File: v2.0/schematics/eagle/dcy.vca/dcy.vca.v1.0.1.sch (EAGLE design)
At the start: 104 parts, among them IC1 LM324N, IC2 4001N, IC3 TL074P, IC4 4001N, IC5 LM324N, IC6 TL074P

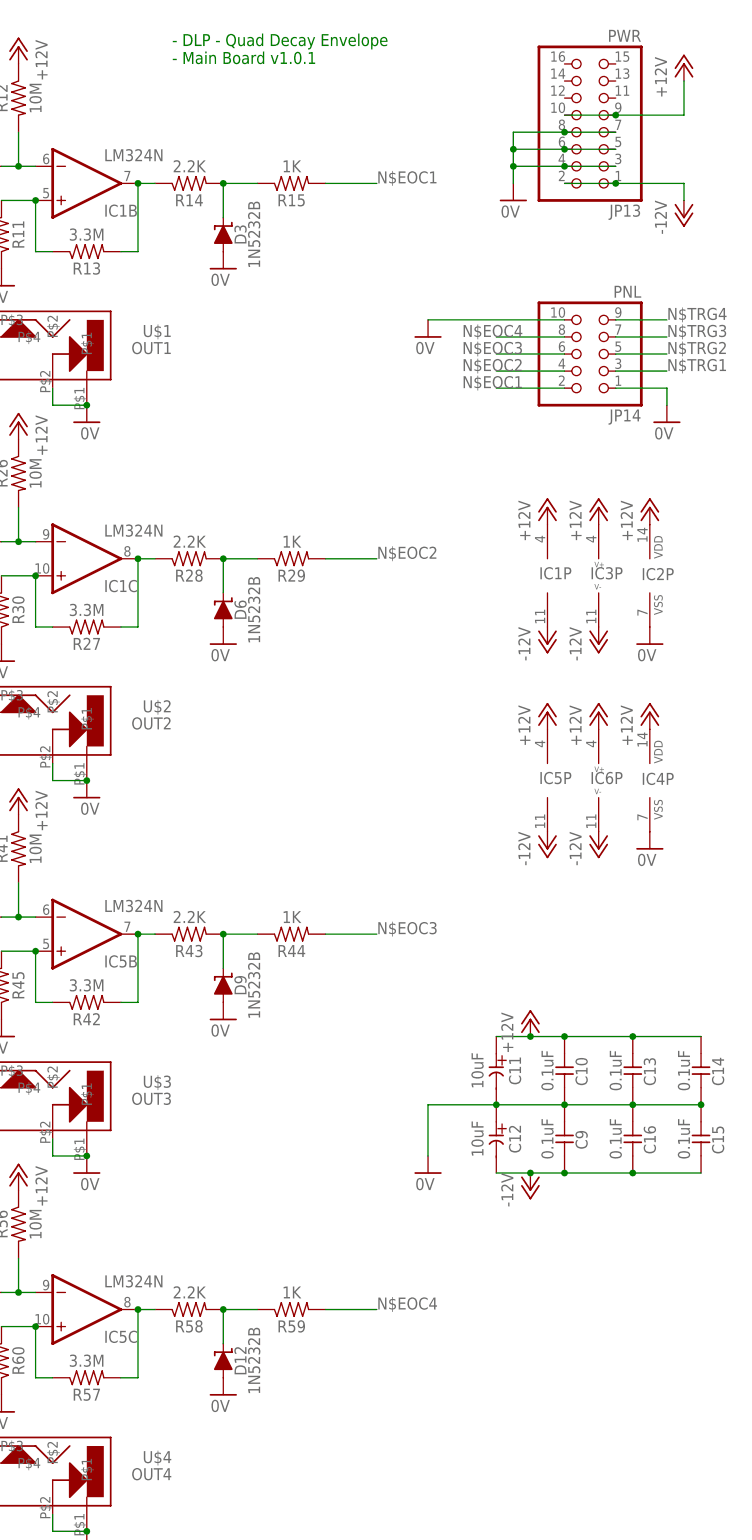
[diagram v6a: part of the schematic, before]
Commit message: Added panel board for quad decay and routed main and pnl
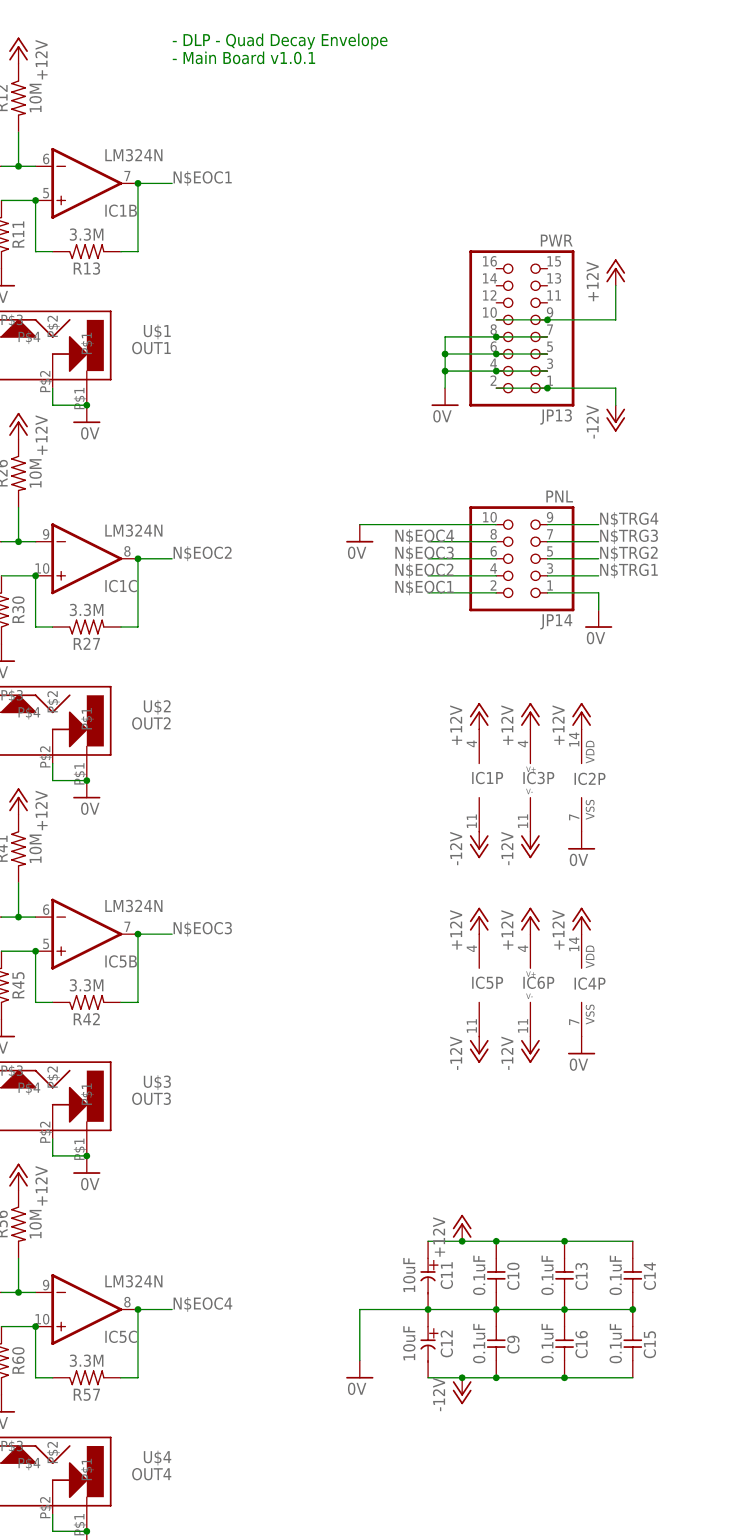
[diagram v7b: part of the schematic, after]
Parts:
- removed D12, D3, D6, D9: 1N5232B, _common:1N5232B
- removed R14, R28, R43, R58: 2.2K, _common:R
- removed R15, R29, R44, R59: 1K, _common:R
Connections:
- removed net N$35: IC1C.OUT, R27.2, R28.1
- removed net N$36: D6.C, R28.2, R29.1
- removed net N$5: IC1B.OUT, R13.2, R14.1
- removed net N$54: IC5B.OUT, R42.2, R43.1
- removed net N$55: D9.C, R43.2, R44.1
- removed net N$6: D3.C, R14.2, R15.1
- removed net N$74: IC5C.OUT, R57.2, R58.1
- removed net N$75: D12.C, R58.2, R59.1
- net 0V: no longer D12.A, D3.A, D6.A, D9.A
- net N$EOC1: now also IC1B.OUT, R13.2; no longer R15.2
- net N$EOC2: now also IC1C.OUT, R27.2; no longer R29.2
- net N$EOC3: now also IC5B.OUT, R42.2; no longer R44.2
- net N$EOC4: now also IC5C.OUT, R57.2; no longer R59.2
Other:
- moved on the sheet: C10, C11, C12, C13, C14, C15, C16, C9, IC1P, IC2P, IC3P, IC4P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

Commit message: Flipped oritentaiton of panel board Changed power header to 2x5 hearder
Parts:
- JP13: device pinhead:PINHD-2X8 -> pinhead:PINHD-2X5
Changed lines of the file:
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@@
 <part name="R60" library="_common" deviceset="R" device="" value="3.3M"/>
 <part name="GND50" library="supply1" deviceset="0V" device=""/>
-<part name="JP13" library="pinhead" deviceset="PINHD-2X8" device="" value="PWR"/>
+<part name="JP13" library="pinhead" deviceset="PINHD-2X5" device="" value="PWR"/>
 <part name="P+15" library="supply1" deviceset="+12V" device=""/>
 <part name="P-5" library="supply1" deviceset="-12V" device=""/>
@@
 <instance part="R60" gate="G$1" x="-93.98" y="-58.42" rot="MR90"/>
 <instance part="GND50" gate="1" x="-93.98" y="-66.04"/>
-<instance part="JP13" gate="A" x="-15.24" y="93.98" rot="R180"/>
+<instance part="JP13" gate="A" x="-15.24" y="91.44" rot="R180"/>
 <instance part="P+15" gate="1" x="-2.54" y="104.14"/>
 <instance part="P-5" gate="1" x="-2.54" y="81.28"/>
